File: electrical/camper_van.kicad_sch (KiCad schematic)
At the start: 54 parts, among them K1 Relay 200A, K2 Relay 200A, K3 Relay 250A, K4 Relay 250A, K5 Relay 1A, Q1 BC107, Q2 BC107, SW1 Solar Panel 1, SW2 Solar Panel 2, SW3 Swap DC-DC Charger, SW4 Battery 2, SW5 Isolate Battery

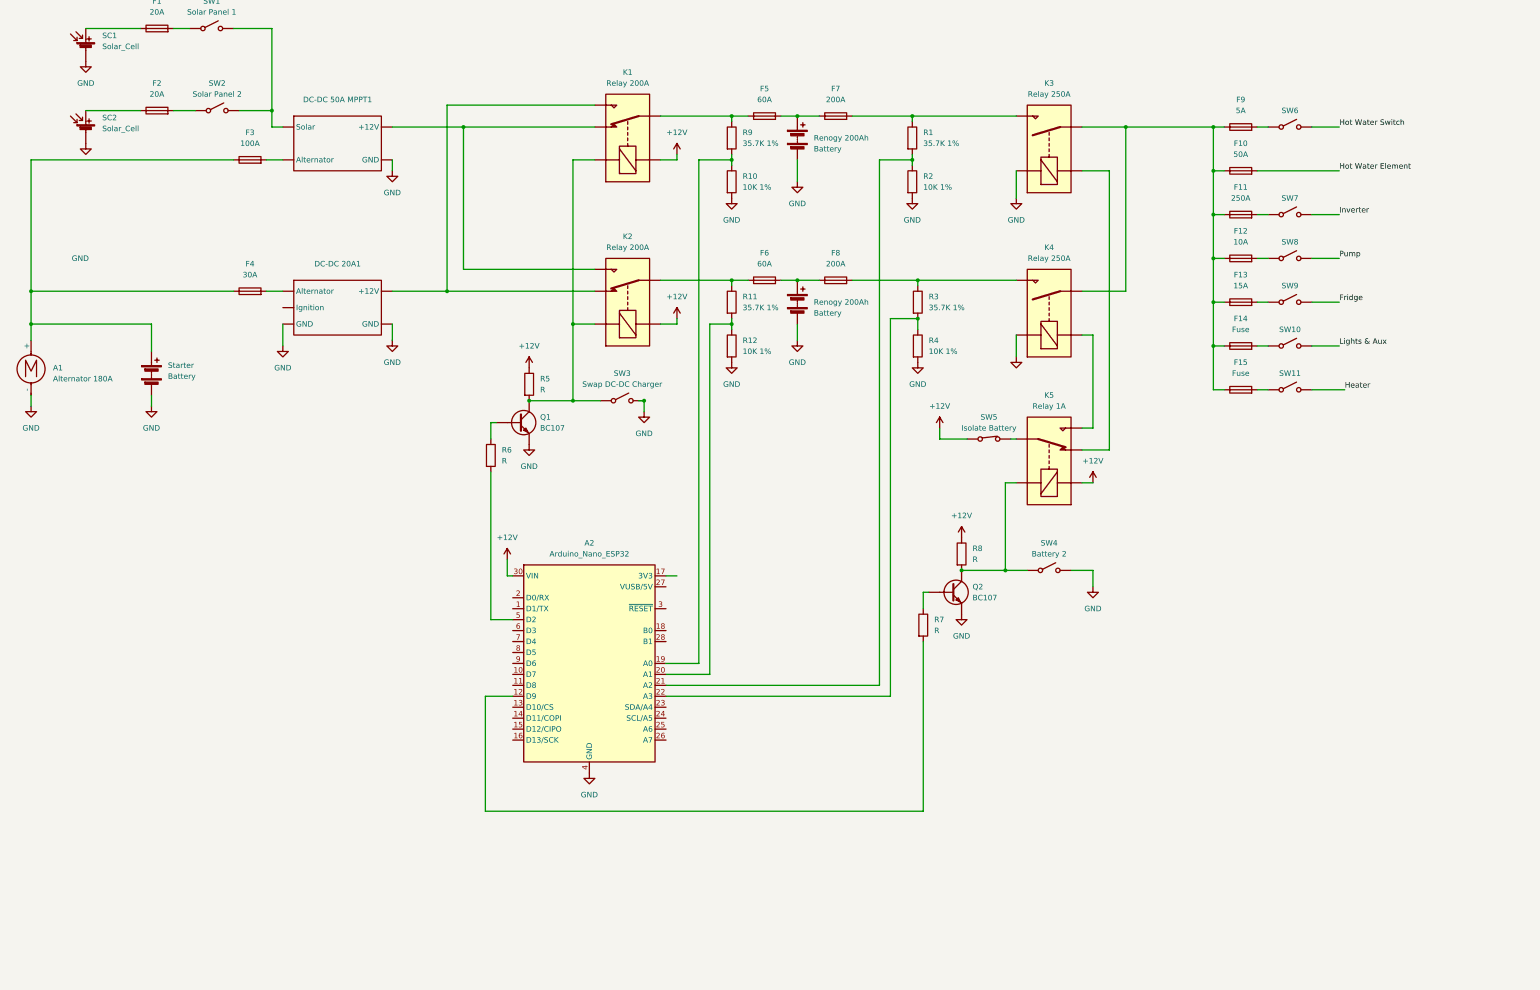
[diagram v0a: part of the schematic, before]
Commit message: Added flow sensors and RS485
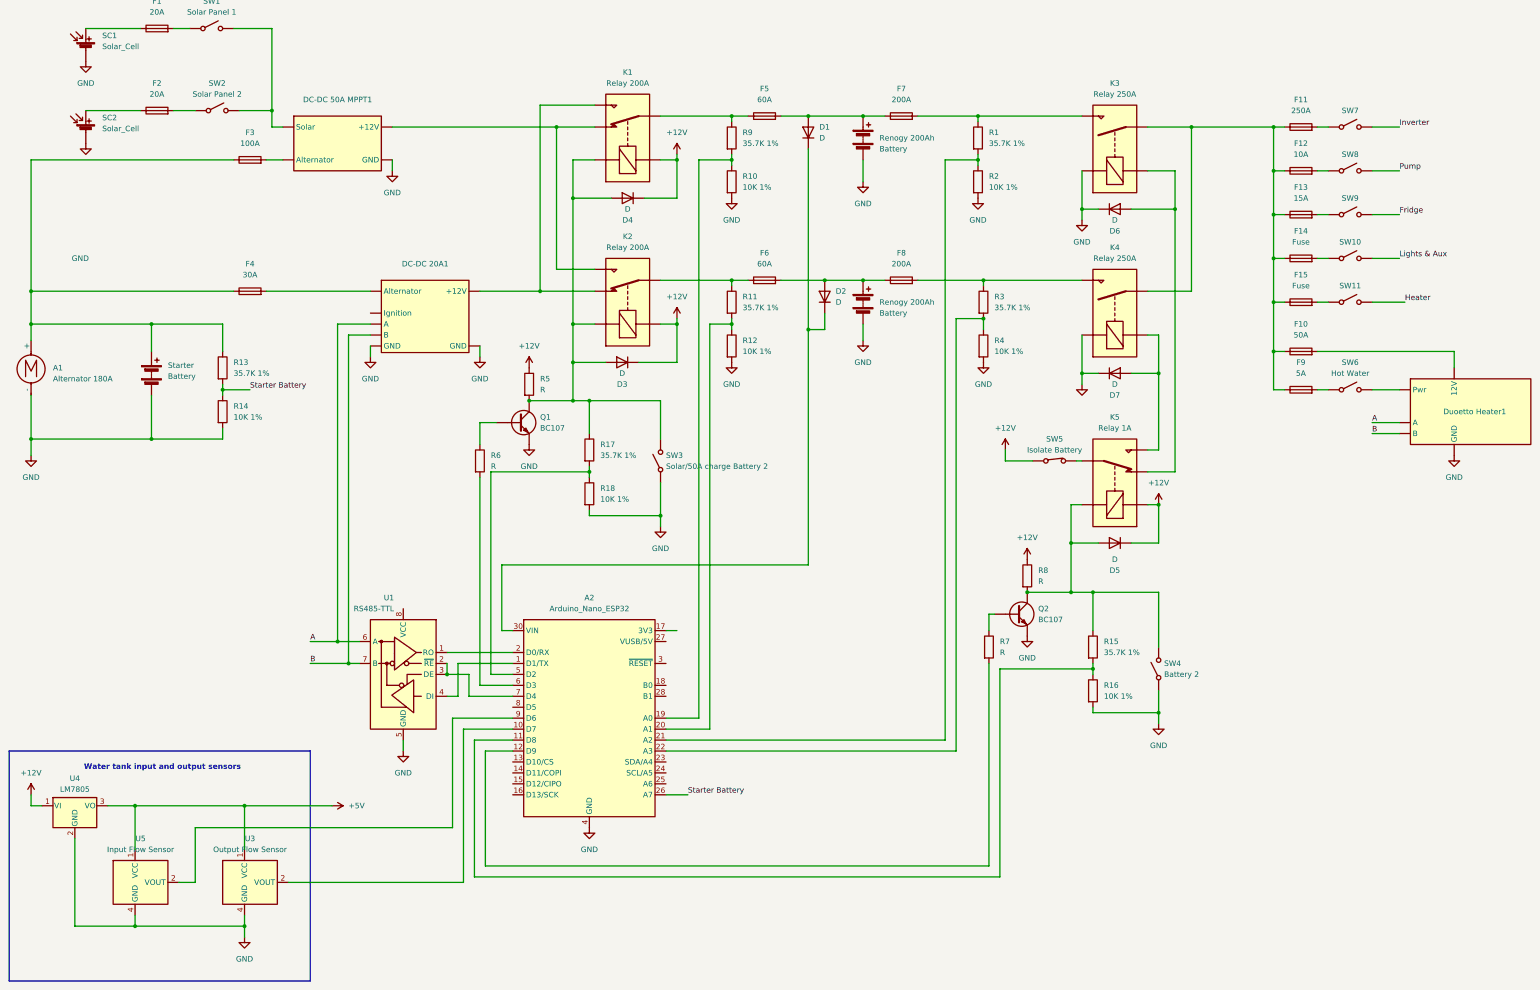
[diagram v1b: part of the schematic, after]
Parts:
- added D1, D2, D3, D4, D5, D6, D7: D, symbol Device:D
- added Duoetto Heater1: ~, symbol camper_van:Duoetto
- added R13, R15, R17: 35.7K 1%, symbol Device:R
- added R14, R16, R18: 10K 1%, symbol Device:R
- added U1: RS485-TTL, Package_SO:SOIC-8_3.9x4.9mm_P1.27mm, symbol Interface_UART:ISL3178E
- added U3: Output Flow Sensor, Sensor_Current:Allegro_SIP-4, symbol Sensor_Current:A1363xKTTN-1
- added U4: LM7805, Package_TO_SOT_THT:TO-220-3_Vertical, symbol Regulator_Linear:LM7805_TO220
- added U5: Input Flow Sensor, Sensor_Current:Allegro_SIP-4, symbol Sensor_Current:A1363xKTTN-1
- SW3: value Swap DC-DC Charger -> Solar/50A charge Battery 2
- SW6: value ~ -> Hot Water
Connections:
- net +12V: now also D3.1 (K), D4.1 (K), D5.1 (K), U4.1 (VI); no longer A2.30 (VIN)
- net GND: now also SW3.1 (A), SW4.1 (A), D6.1 (K), D7.1 (K), Duoetto Heater1. (GND), R14.2, R16.2, R18.2, U1.5 (GND), U3.4 (GND), U4.2 (GND), U5.4 (GND); no longer SW3.2 (B), SW4.2 (B)
- net at K5.A2, Q2.3 (C), R8.2: now also SW4.2 (B), D5.2 (A), R15.1; no longer SW4.1 (A)
- net at K3.A2, K5.12: now also D6.2 (A)
- net at K1.A1, K2.A1, Q1.3 (C)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: now also SW3.2 (B), D3.2 (A), D4.2 (A), R17.1; no longer SW3.1 (A)
- net at F6.2, F8.1, Renogy 200Ah.1 (+): now also D2.2 (A)
- net at K4.A2, K5.14: now also D7.2 (A)
- net at A2.5 (D2): now also R17.2, R18.1; no longer R6.2
- net at F5.2, F7.1, Renogy 200Ah.1 (+): now also D1.2 (A)
- net at A1.1 (+), F3.1, F4.1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: now also R13.1
- net at A2.1 (D1/TX): now also U1.4 (DI)
- net at A2.10 (D7): now also U3.2 (VOUT)
- net at A2.11 (D8): now also R15.2, R16.1
- net at A2.2 (D0/RX): now also U1.1 (RO)
- net Starter Battery: now reaches A2.26 (A7)
- net Starter Battery: now also R13.2, R14.1
- net at A2.6 (D3): now also R6.2
- net at A2.7 (D4): now also U1.2 (~{RE}), U1.3 (DE)
- net at A2.9 (D6): now also U5.2 (VOUT)
- net Hot Water Element: no longer names the net of F10.2
- net Hot Water Element: now also Duoetto Heater1. (GND)
- net Hot Water Switch: no longer names the net of SW6.2 (B)
- net Hot Water Switch: now also Duoetto Heater1. (GND)
- new net: A2.30 (VIN), D1.1 (K), D2.1 (K)
- new net +5V: U3.1 (VCC), U4.3 (VO), U5.1 (VCC)
- new net A: DC-DC 20A1. (GND), Duoetto Heater1. (GND), U1.6 (A)
- new net B: DC-DC 20A1. (GND), Duoetto Heater1. (GND), U1.7 (B)
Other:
- note added: "Water tank input and output sensors"
- moved on the sheet: A2, F10, F11, F12, F13, F14, F15, F7, F8, F9, K3, K4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

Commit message: commit
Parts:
- removed D1, D2, D3, D4, D5, D6, D7: D, symbol Device:D
- removed K5: Relay 1A, symbol Relay:Relay_SPDT
- removed R5, R8: R, symbol Device:R
- removed SW5: Isolate Battery, symbol Switch:SW_SPST_1
- added A3: Arduino_Nano_v3.x, Module:Arduino_Nano, symbol MCU_Module:Arduino_Nano_v3.x
- added C1: 0.33uF, symbol Device:C_Polarized_Small_US
- added C2: 0.1uF, symbol Device:C_Polarized_Small_US
- added D1, D3, D4, D7, D8: 1N4001, Diode_THT:D_DO-41_SOD81_P10.16mm_Horizontal, symbol Diode:1N4001
- added D5, D6: 1N914, Diode_THT:D_DO-35_SOD27_P7.62mm_Horizontal, symbol Diode:1N914
- added J1: Starter Battery, symbol Connector:Conn_01x01_Socket
- added J10: Fuse and Switch Box, symbol Connector:Conn_01x06_Pin
- added J11: Fuse and Switch Box, symbol Connector:Conn_01x06_Socket
- added J12: Duoetto Remote, symbol Connector:Conn_01x02_Socket
- added J2: Duoetto Remote, symbol Connector:Conn_01x02_Pin
- added J3: ~, symbol Connector:Conn_01x03_Pin
- added J4: Input Flow Sensor, symbol Connector:Conn_01x03_Socket
- added J5: Conn_01x03_Pin, symbol Connector:Conn_01x03_Pin
- added J6: Output Flow Sensor, symbol Connector:Conn_01x03_Socket
- added J7: Battery Box, symbol Connector:Conn_01x16_Socket
- added J8: Battery Box, symbol Connector:Conn_01x16_Pin
- added J9: Starter Battery, symbol Connector:Conn_01x01_Pin
- added K4, K8: G5Q-1, Relay_THT:Relay_SPDT_Omron-G5Q-1, symbol Relay:G5Q-1
- added M1: Battery Box Fan, symbol Motor:Fan
- added Q2: D4184, symbol Simulation_SPICE:NMOS
- added Q3: BC337, Package_TO_SOT_THT:TO-18-3, symbol Transistor_BJT:BC107
- added R13: 150, symbol Device:R
- added R19, R21: 4k7, symbol Device:R
- added R2: 1k, symbol Device:R
- added R20: 100, symbol Device:R
- added SW9: 12V Power On/Off, symbol Switch:SW_SPST
- added U4: DS18B20, Package_TO_SOT_THT:TO-92_Inline, symbol Sensor_Temperature:DS18B20
- added U6: IPS 3.5" Display, Display:CR2013-MI2120, symbol camper_van:Display IPS 3.5{dblquote}
- added U7: PC817, Package_DIP:DIP-4_W7.62mm, symbol Isolator:PC817
- Duoetto_Heater1: renamed from Duoetto Heater1
- Q1: value BC107 -> BC337
- Q4: renamed from Q2; value BC107 -> BC337
- R1: renamed from R6; value R -> 150
- R16: renamed from R7; value R -> 150
- Renogy 200Ah1: renamed from Renogy 200Ah
- Renogy 200Ah2: renamed from Renogy 200Ah
- SW10: renamed from SW4; value Battery 2 -> Battery 2 On/Off
- renumbered F3 to F1, F14 to F10, F15 to F11, F10 to F12, F9 to F13, F1 to F14, F2 to F15, F4 to F2, F5 to F3, F6 to F4, F7 to F5, F8 to F6, F11 to F7, F12 to F8, F13 to F9, K1 to K2, K2 to K3, K3 to K5, K4 to K6, R2 to R10, R3 to R11, R4 to R12, R13 to R14, R14 to R15, R15 to R17, R16 to R18, R17 to R3, R18 to R4, R9 to R5, R10 to R6, R11 to R7, R12 to R8, R1 to R9, SC2 to SC1, SC1 to SC2, SW3 to SW11, SW7 to SW3, SW8 to SW4, SW9 to SW5, SW10 to SW6, SW11 to SW7, SW6 to SW8, Starter to Starter1, U5 to U1, U3 to U2, U1 to U3, U4 to U5
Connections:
- net +12V: now also F10.1, F11.1, F12.1, F13.1, F7.1, F8.1, F9.1, K5.14, K6.14, D1.1 (K), D5.1 (K), D6.1 (K), J7.15 (Pin_15), J8.15 (Pin_15), K4.1, K4.2, K8.1, R21.1; no longer U5.1 (VI)
- net +5V: now also C2.1, J3.1 (Pin_1), J5.1 (Pin_1), J8.5 (Pin_5); no longer U1.1 (VCC), U2.1 (VCC)
- net GND: now also K5.A2, K6.A2, A3.29 (GND), A3.4 (GND), C1.2, C2.2, D7.1 (K), D8.1 (K), J10.4 (Pin_4), J10.6 (Pin_6), J3.3 (Pin_3), J5.3 (Pin_3), J7.16 (Pin_16), J8.16 (Pin_16), M1.2 (-), Q2.3 (S), Q3.1 (E), R19.2, U4.1 (GND), U6.2 (GND), U7.2; no longer K5.A1, K6.A1, SW10.1 (A), SW11.1 (A), U1.4 (GND), U2.4 (GND)
- net Battery 2 On/Off Switch Sensor: now reaches A2.11 (D8), R17.2, R18.1
- net at Q4.2 (B): now also R16.2; no longer R16.1
- net at Q4.3 (C), R17.1: now also D6.2 (A), J10.3 (Pin_3), K8.5; no longer SW10.2 (B)
- net at F3.1, K2.11: now also J7.7 (Pin_7); no longer R5.1
- net at F4.2, F6.1, Renogy 200Ah2.1 (+): now also J7.10 (Pin_10)
- net ignition: now reaches DC-DC 20A1. (GND)
- net at F4.1, K3.11: now also J7.8 (Pin_8); no longer R7.1
- net at A1.1 (+), F1.1, F2.1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: now also J1.1 (Pin_1); no longer R14.1
- net at A2.10 (D7): now also J5.2 (Pin_2); no longer U2.2 (VOUT)
- net Battery 2 On/Off: now reaches A2.12 (D9)
- net Battery 2 On/Off: now also R16.1; no longer R16.2
- net 12V Power On/Off: now reaches A2.13 (D10/CS)
- net 12V Power On/Off: now also R13.2
- net at A2.16 (D13/SCK): now also R2.1
- net Battery Box Temp Sensor: now reaches A2.23 (SDA/A4)
- net Battery Box Temp Sensor: now also J8.4 (Pin_4)
- net VIN: now reaches A2.30 (VIN)
- net VIN: now also U5.1 (VI), C1.1, D3.1 (K), D4.1 (K)
- net at A2.9 (D6): now also J3.2 (Pin_2); no longer U1.2 (VOUT)
- net at SW2.1 (A): now also DC-DC 50A MPPT1. (GND), SW1.1 (A); no longer F15.2
- net at F14.2: now also SW1.2 (B); no longer SW1.1 (A)
- removed net A: DC-DC 20A1. (GND), Duoetto_Heater1. (GND), U3.6 (A)
- removed net B: DC-DC 20A1. (GND), Duoetto_Heater1. (GND), U3.7 (B)
- net Starter Battery renamed Starter Battery Sensor
- new net: F5.2, K5.13
- new net: J7.13 (Pin_13), K5.A1
- new net: J7.3 (Pin_3), M1.1 (+)
- new net: D4.2 (A), J8.8 (Pin_8)
- new net: Q2.2 (G), R19.1, R20.2
- new net: J7.6 (Pin_6), K2.A1, K3.A1
- new net: Q3.2 (B), R13.1
- new net: D5.2 (A), K4.5, Q3.3 (C)
- new net: F6.2, J7.12 (Pin_12), K6.13
- new net: D3.2 (A), J8.7 (Pin_7)
- new net: DC-DC 20A1. (GND), J7.1 (Pin_1)
- new net: DC-DC 20A1. (GND), J7.2 (Pin_2)
- new net: R2.2, U7.1
- new net: J11.1 (Pin_1), SW9.1 (A)
- new net: J11.2 (Pin_2), SW9.2 (B)
- new net: J11.3 (Pin_3), SW10.1 (A)
- new net: J11.4 (Pin_4), SW10.2 (B)
- new net: J11.5 (Pin_5), SW11.1 (A)
- new net: J11.6 (Pin_6), SW11.2 (B)
- new net: J7.14 (Pin_14), K6.A1
- new net: J10.1 (Pin_1), K8.2
- new net: J10.2 (Pin_2), K4.3
- new net: F15.2, SW2.2 (B)
- new net: R20.1, U7.3
- new net: Duoetto_Heater1. (GND), J12.1 (Pin_1)
- new net: Duoetto_Heater1. (GND), J12.2 (Pin_2)
- new net: J7.4 (Pin_4), U4.2 (DQ)
- new net: J7.5 (Pin_5), U4.3 (V_{DD})
- new net: J6.1 (Pin_1), U2.1 (VCC)
- new net: J6.2 (Pin_2), U2.2 (VOUT)
- new net: J6.3 (Pin_3), U2.4 (GND)
- new net: J9.1 (Pin_1), R14.1
- new net: J4.1 (Pin_1), U1.1 (VCC)
- new net: J4.2 (Pin_2), U1.2 (VOUT)
- new net: J4.3 (Pin_3), U1.4 (GND)
- new net: R21.2, U7.4
- new net: A3.14 (D11), U6.6 (MOSI)
- new net: A3.16 (D13), U6.7 (SCK)
- new net: A3.15 (D12), U6.9 (MISO)
- new net Battery 1: D8.2 (A), J8.13 (Pin_13), K8.4
- new net Battery 1 In Sensor: J8.9 (Pin_9), R5.1
- new net Battery 1 Out Sensor: J8.11 (Pin_11), R9.1
- new net Battery 2: D7.2 (A), J8.14 (Pin_14), K8.3
- new net Battery 2 In Sensor: J8.10 (Pin_10), R7.1
- new net Battery 2 Out Sensor: J8.12 (Pin_12), R11.1
- new net Battery Box Fan: J8.3 (Pin_3), Q2.1 (D)
- new net CTP_SCL: A3.24 (A5), U6.10 (CTP_SCL)
- new net CTP_SDA: A3.23 (A4), U6.12 (CTP_SDA)
- new net RS485 Rx: A3.2 (D0/RX), J2.1 (Pin_1), J8.1 (Pin_1), U3.6 (A)
- new net RS485 Tx: A3.1 (D1/TX), J2.2 (Pin_2), J8.2 (Pin_2), U3.7 (B)
- new net Solar Switch: D1.2 (A), J10.5 (Pin_5), J8.6 (Pin_6), Q1.3 (C), R3.1
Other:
- note added: "12V Power On/Off"
- note added: "Battery 2 On/Off"
- note added: "Battery Box"
- note added: "Solar/50A charge Battery 2"
- note added: "Switch and Fuse Panel"
- note added: "Water tank input and output flow sensors"
- note removed: "Water tank input and output sensors"
- moved on the sheet: A1, A2, DC-DC 20A1, DC-DC 50A MPPT1, Duoetto_Heater1, F1, F10, F11, F12, F13, F14, F15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

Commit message: updated
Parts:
- removed F11: Fuse, symbol Device:Fuse
- removed SW7: ~, symbol Switch:SW_SPST
- added D10, D2, D9: 4V7, Diode_THT:D_DO-41_SOD81_P10.16mm_Horizontal, symbol Diode:1N47xxA
- added R22, R23, R24, R25, R27, R28, R30, R31, R33, R34, R36, R37, R39, R43: 10k, symbol Device:R
- added R26, R29, R32, R35, R38: 6k2, symbol Device:R
- added R40, R41: ~, symbol Device:R
- SW3: value ~ -> Inverter
- SW4: value ~ -> Pump
- SW5: value ~ -> Fridge
- SW6: value ~ -> Lights & Aux
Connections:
- net +12V: now also R25.1, R28.1, R31.1, R34.1, R37.1, R40.1
- net Fridge: now also R35.2, R36.1
- net GND: now also D10.2 (A), D2.2 (A), D9.2 (A), R27.2, R30.2, R33.2, R36.2, R39.2, R41.2, R43.2
- net Inverter: now also R26.2, R27.1
- net Lights & Aux: now also R38.2, R39.1
- net Pump: now also R29.2, R30.1
- net at F14.1, SC2.1 (+): now also R23.2
- net at F10.2, SW6.1 (A): now also R37.2, R38.1
- net at F8.2, SW4.1 (A): now also R28.2, R29.1
- net at F7.2, SW3.1 (A): now also R25.2, R26.1
- net at F15.1, SC1.1 (+): now also R22.2
- net DuoettoFS: now reaches Duoetto_Heater1. (GND), SW8.2 (B)
- net DuoettoFS: now also R32.2, R33.1
- net Duoetto50AFuse: now reaches Duoetto_Heater1. (GND), F12.2
- net Duoetto50AFuse: now also R43.1
- net at F13.2, SW8.1 (A): now also R31.2, R32.1
- net at F14.2, SW1.2 (B): now also R24.1
- net at F9.2, SW5.1 (A): now also R34.2, R35.1
- new net: D9.1 (K), R24.2
- new net: D10.1 (K), R22.1
- new net: D2.1 (K), R23.1
- new net ADC Input: R40.2, R41.1
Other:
- moved on the sheet: A3, Duoetto_Heater1, F10, F12, F13, F15, F7, F8, F9, J11, J12, SC1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

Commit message: Design has been split into 3x modules
- management module
- fuse and switch modules
- display module
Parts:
- removed A2: Arduino_Nano_ESP32, Module:Arduino_Nano, symbol MCU_Module:Arduino_Nano_ESP32
- removed A3: Arduino_Nano_v3.x, Module:Arduino_Nano, symbol MCU_Module:Arduino_Nano_v3.x
- removed C1: 0.33uF, symbol Device:C_Polarized_Small_US
- removed C2: 0.1uF, symbol Device:C_Polarized_Small_US
- removed D1, D3, D4, D7, D8: 1N4001, Diode_THT:D_DO-41_SOD81_P10.16mm_Horizontal, symbol Diode:1N4001
- removed D10, D2, D9: 4V7, Diode_THT:D_DO-41_SOD81_P10.16mm_Horizontal, symbol Diode:1N47xxA
- removed D5, D6: 1N914, Diode_THT:D_DO-35_SOD27_P7.62mm_Horizontal, symbol Diode:1N914
- removed F10: Fuse, symbol Device:Fuse
- removed F12: 50A, symbol Device:Fuse
- removed F13: 5A, symbol Device:Fuse
- removed F14, F15: 20A, symbol Device:Fuse
- removed F7: 250A, symbol Device:Fuse
- removed F8: 10A, symbol Device:Fuse
- removed F9: 15A, symbol Device:Fuse
- removed J10: Fuse and Switch Box, symbol Connector:Conn_01x06_Pin
- removed J11: Fuse and Switch Box, symbol Connector:Conn_01x06_Socket
- removed J2: Duoetto Remote, symbol Connector:Conn_01x02_Pin
- removed J3: ~, symbol Connector:Conn_01x03_Pin
- removed J9: Starter Battery, symbol Connector:Conn_01x01_Pin
- removed K4, K8: G5Q-1, Relay_THT:Relay_SPDT_Omron-G5Q-1, symbol Relay:G5Q-1
- removed Q1, Q3, Q4: BC337, Package_TO_SOT_THT:TO-18-3, symbol Transistor_BJT:BC107
- removed Q2: D4184, symbol Simulation_SPICE:NMOS
- removed R1, R13, R16: 150, symbol Device:R
- removed R10, R12, R15, R18, R4, R6, R8: 10K 1%, symbol Device:R
- removed R11, R14, R17, R3, R5, R7, R9: 35.7K 1%, symbol Device:R
- removed R19, R21: 4k7, symbol Device:R
- removed R2: 1k, symbol Device:R
- removed R20: 100, symbol Device:R
- removed R22, R23, R24, R25, R27, R28, R30, R31, R33, R34, R36, R37, R39, R43: 10k, symbol Device:R
- removed R26, R29, R32, R35, R38: 6k2, symbol Device:R
- removed R40, R41: ~, symbol Device:R
- removed SW1: Solar Panel 1, symbol Switch:SW_SPST
- removed SW10: Battery 2 On/Off, symbol Switch:SW_SPST
- removed SW11: Solar/50A charge Battery 2, symbol Switch:SW_SPST
- removed SW2: Solar Panel 2, symbol Switch:SW_SPST
- removed SW3: Inverter, symbol Switch:SW_SPST
- removed SW4: Pump, symbol Switch:SW_SPST
- removed SW5: Fridge, symbol Switch:SW_SPST
- removed SW6: Lights & Aux, symbol Switch:SW_SPST
- removed SW8: Hot Water, symbol Switch:SW_SPST
- removed SW9: 12V Power On/Off, symbol Switch:SW_SPST
- removed U3: RS485-TTL, Package_SO:SOIC-8_3.9x4.9mm_P1.27mm, symbol Interface_UART:ISL3178E
- removed U5: LM7805, Package_TO_SOT_THT:TO-220-3_Vertical, symbol Regulator_Linear:LM7805_TO220
- removed U6: IPS 3.5" Display, Display:CR2013-MI2120, symbol camper_van:Display IPS 3.5{dblquote}
- removed U7: PC817, Package_DIP:DIP-4_W7.62mm, symbol Isolator:PC817
- added J2: Ignition, symbol Connector:Conn_01x01_Socket
- added J6: Output Flow Sensor, Connector_Molex:CONN_SD-172648-0000_02_MOL, symbol Connector:Conn_01x03_Pin
- J5: value Conn_01x03_Pin -> Input Flow Sensor; footprint (none) -> Connector_Molex:CONN_SD-172648-0000_02_MOL
- J8: footprint (none) -> Connector_Molex:Molex_Mini-Fit_Jr_5569-16A2_2x08_P4.20mm_Horizontal
- renumbered J4 to J3, J6 to J4, J12 to J9, K2 to K1, K3 to K2, K5 to K3, K6 to K4, U4 to U3
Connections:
- net +5V: now also J3.1 (Pin_1), J4.1 (Pin_1), J7.5 (Pin_5), U1.1 (VCC), U2.1 (VCC), U3.3 (V_{DD}); no longer J5.1 (Pin_1), J8.5 (Pin_5)
- net GND: now also DC-DC 20A1.5 (GND), DC-DC 20A1.7 (GND), DC-DC 50A MPPT1.4 (GND), Duoetto_Heater1.5 (GND), J3.3 (Pin_3), J4.3 (Pin_3), U1.4 (GND), U2.4 (GND), J6.3 (Pin_3); no longer DC-DC 20A1. (GND), DC-DC 50A MPPT1. (GND), Duoetto_Heater1. (GND)
- net Fuse and Switch Module/Solar 1: now reaches SC2.1 (+)
- net at F5.2, K3.13: now also J7.11 (Pin_11)
- net Management Module/Battery 2 Vin: now reaches J8.8 (Pin_8)
- net at K1.12, K2.14: now also DC-DC 50A MPPT1.3 (+12V); no longer DC-DC 50A MPPT1. (GND)
- net at K1.14, K2.12: now also DC-DC 20A1.6 (+12V); no longer DC-DC 20A1. (GND)
- net Management Module/Battery 1 Vin: now reaches J8.7 (Pin_7)
- net at J7.1 (Pin_1): now also DC-DC 20A1.3 (A); no longer DC-DC 20A1. (GND)
- net at J7.2 (Pin_2): now also DC-DC 20A1.4 (B); no longer DC-DC 20A1. (GND)
- net at F2.2: now also DC-DC 20A1.1 (Alternator); no longer DC-DC 20A1. (GND)
- net Fuse and Switch Module/Solar 2: now reaches SC1.1 (+)
- net at F3.2, F5.1, Renogy 200Ah1.1 (+): now also J7.9 (Pin_9)
- net Management Module/Input Flow Sensor: now reaches J5.2 (Pin_2)
- net at F1.2: now also DC-DC 50A MPPT1.2 (Alternator); no longer DC-DC 50A MPPT1. (GND)
- net at J9.1 (Pin_1): now also Duoetto_Heater1.2 (A); no longer Duoetto_Heater1. (GND)
- net at J9.2 (Pin_2): now also Duoetto_Heater1.3 (B); no longer Duoetto_Heater1. (GND)
- net Battery 1 renamed Management Module/Battery 1 Relay
- net Battery 1 In Sensor renamed Management Module/Battery 1 In Sensor
- net Battery 1 Out Sensor renamed Management Module/Battery 1 Out Sensor
- net Battery 2 renamed Management Module/Battery 2 Relay
- net Battery 2 In Sensor renamed Management Module/Battery 2 In Sensor
- net Battery 2 Out Sensor renamed Management Module/Battery 2 Out Sensor
- net Battery Box Fan renamed Management Module/Battery Box Fan
- net Battery Box Temp Sensor renamed Management Module/Temperature Sensors
- removed net Duoetto50AFuse: Duoetto_Heater1. (GND)
- removed net DuoettoFS: Duoetto_Heater1. (GND)
- net Solar Switch renamed Fuse and Switch Module/Solar Charge Battery 2
- removed net ignition: DC-DC 20A1. (GND)
- new net: DC-DC 20A1.2 (Ignition), J2.1 (Pin_1)
- new net Fuse and Switch Module/Duoetto 12V: Duoetto_Heater1.4 (12V)
- new net Fuse and Switch Module/Duoetto Power On/Off: Duoetto_Heater1.1 (Pwr)
- new net Management Module/5V: J5.1 (Pin_1), J6.1 (Pin_1), J8.5 (Pin_5)
- new net Management Module/Output Flow Sensor: J6.2 (Pin_2)
- new net Solar Charge: DC-DC 50A MPPT1.1 (Solar)
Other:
- added sheet Fuse and Switch Module (fuse_switch.kicad_sch)
- added sheet Management Module (management_module.kicad_sch)
- added sheet Touch Screen Display (display.kicad_sch)
- note removed: "12V Power On/Off"
- note removed: "Battery 2 On/Off"
- note removed: "Solar/50A charge Battery 2"
- note removed: "Switch and Fuse Panel"
- moved on the sheet: J3, J4, J9, SC1, SC2, U1, U2
